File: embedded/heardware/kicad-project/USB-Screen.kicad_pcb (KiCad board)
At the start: 2 copper layers, 32 x 34 mm, 19 parts, among them J1 USB_B_Micro, J2 Conn_01x04, U1 ZJY154T-PG04, U2 CH551, U3 XC662

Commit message: 微调，打样
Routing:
- net GND: vias 29 -> 35
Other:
- board text added: "5V"
- board text added: "DM"
- board text added: "DP"
- board text added: "GND"
- board text added: "USB-Screen 1.0"

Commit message: 更正背光电路
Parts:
- added Q1: NPN, Package_TO_SOT_SMD:SOT-23, F.Cu at (105.7, 100.6)
- added R6: 33R, Resistor_SMD:R_0402_1005Metric, F.Cu at (105.7, 97.9)
- U3: value XC662 -> SC662
- moved R2 4.69 mm to (117.3, 102.2), turned to 0 degrees
- moved C5 1.37 mm to (119.6, 102.2)
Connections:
- R2 pad 2: /PWM -> +5V
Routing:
- net /KEDA: track 15.8 -> 27.1 mm, vias 1 -> 3
- net +5V: track 49.8 -> 57.4 mm, vias 1 -> 3
- net /PWM: track 1.94 -> 6.08 mm, vias 0 -> 2
- net Net-(Q1-Pad2): track 0.00 -> 1.89 mm
- net GND: vias 35 -> 33

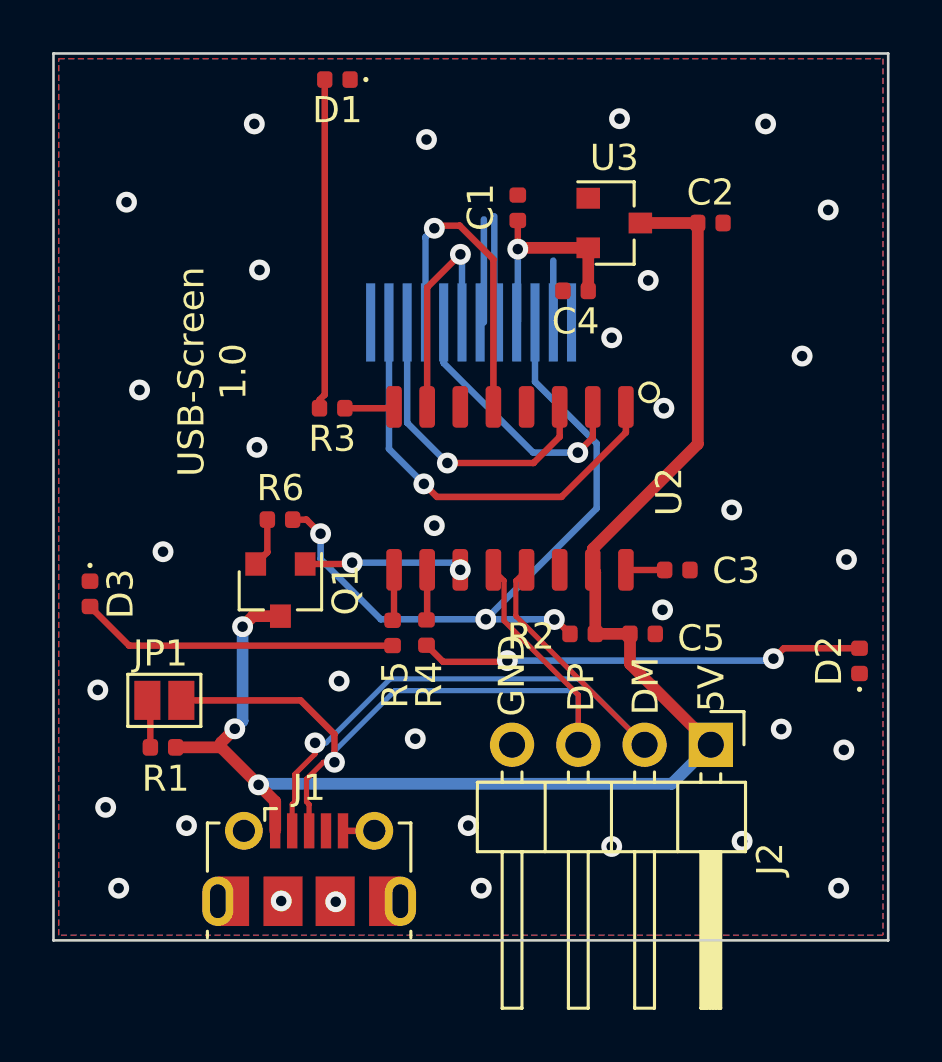
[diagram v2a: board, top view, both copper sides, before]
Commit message: sda、clk加上拉电阻，去掉下载电路焊盘
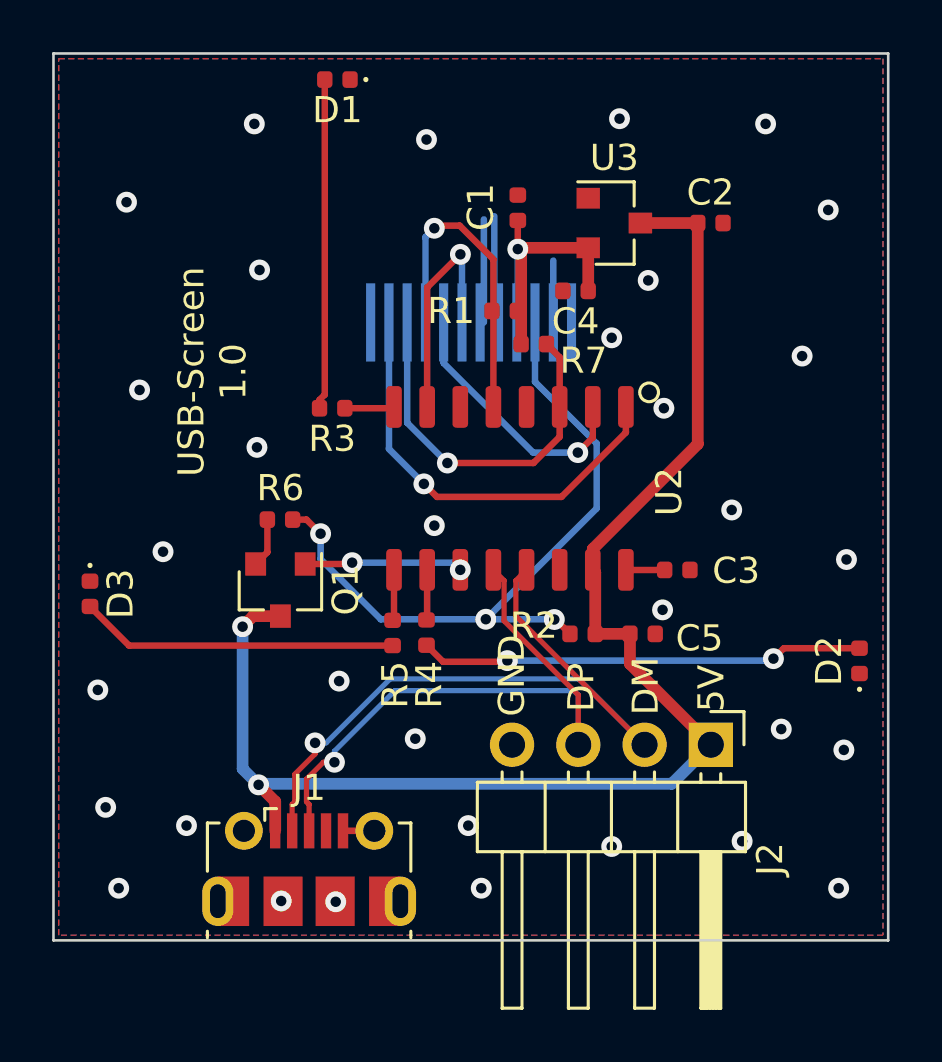
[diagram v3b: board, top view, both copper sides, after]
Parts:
- removed JP1: P3.6 download, Jumper:SolderJumper-2_P1.3mm_Open_Pad1.0x1.5mm
- added R7: 10K, Resistor_SMD:R_0402_1005Metric, F.Cu at (115.4, 91.1)
- moved R1 21.2 mm to (114.3, 89.9)
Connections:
- R1 pad 1: Net-(JP1-Pad2) -> /SCL
- R1 pad 2: +5V -> +3V3
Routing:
- net /USB_D+: track 31.6 -> 24.1 mm
- net +3V3: track 8.30 -> 12.0 mm
- net /SDA: track 11.9 -> 14.5 mm
- net +5V: track 57.4 -> 55.0 mm, vias 3 -> 2
- net Net-(JP1-Pad2): track 1.85 -> 0.00 mm

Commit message: 重新布线
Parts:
- removed R7: 10K, Resistor_SMD:R_0402_1005Metric
- added D4: SS14, Diode_SMD:D_SMA, F.Cu at (118.6, 90.5)
- added D5: SS14, Diode_SMD:D_SMA, F.Cu at (111.0, 90.5)
- added R2: 10K, Resistor_SMD:R_0402_1005Metric, F.Cu at (110.3, 85.4)
- moved R1 5.20 mm to (111.6, 85.4), turned to 270 degrees
- moved C2 3.77 mm to (121.1, 82.9), turned to 90 degrees
- moved U3 2.98 mm to (118.5, 83.5)
- moved C4 2.60 mm to (117.5, 86.5), turned to 270 degrees
- moved C1 2.16 mm to (116.0, 84.2)
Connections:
- R1 pad 1: /SCL -> +3V3
- R1 pad 2: +3V3 -> /SDA
- U2 pad 3: /SDA -> Net-(D4-Pad1)
- U2 pad 5: /SCL -> Net-(D5-Pad1)
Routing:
- net GND: track 11.6 -> 6.68 mm, vias 33 -> 31
- net +5V: track 55.0 -> 59.5 mm
- net +3V3: track 12.0 -> 15.4 mm
- net Net-(D5-Pad1): track 0.00 -> 3.42 mm
- net Net-(D4-Pad1): track 0.00 -> 3.12 mm
- net /SCL: track 12.3 -> 9.27 mm
- net /SDA: track 14.5 -> 15.7 mm
- net Net-(D1-Pad2): track 12.7 -> 13.8 mm
- net /DC: track 9.01 -> 9.80 mm
